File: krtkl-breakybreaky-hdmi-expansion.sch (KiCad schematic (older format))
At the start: 6 parts

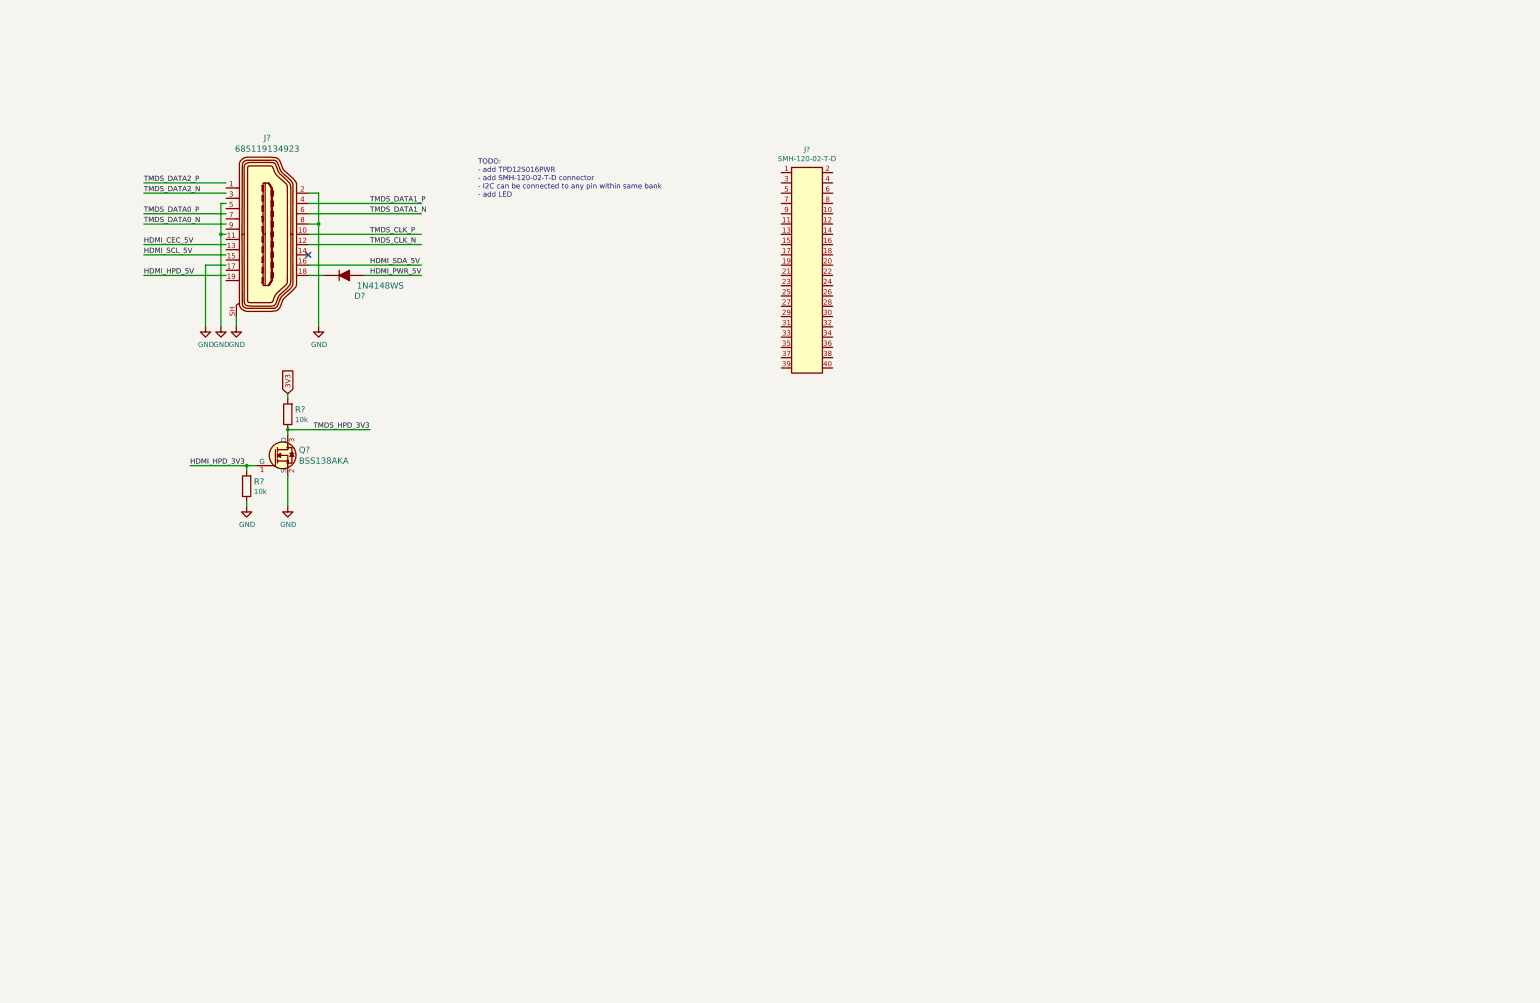
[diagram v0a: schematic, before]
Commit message: Finished schematics, added components to PCB
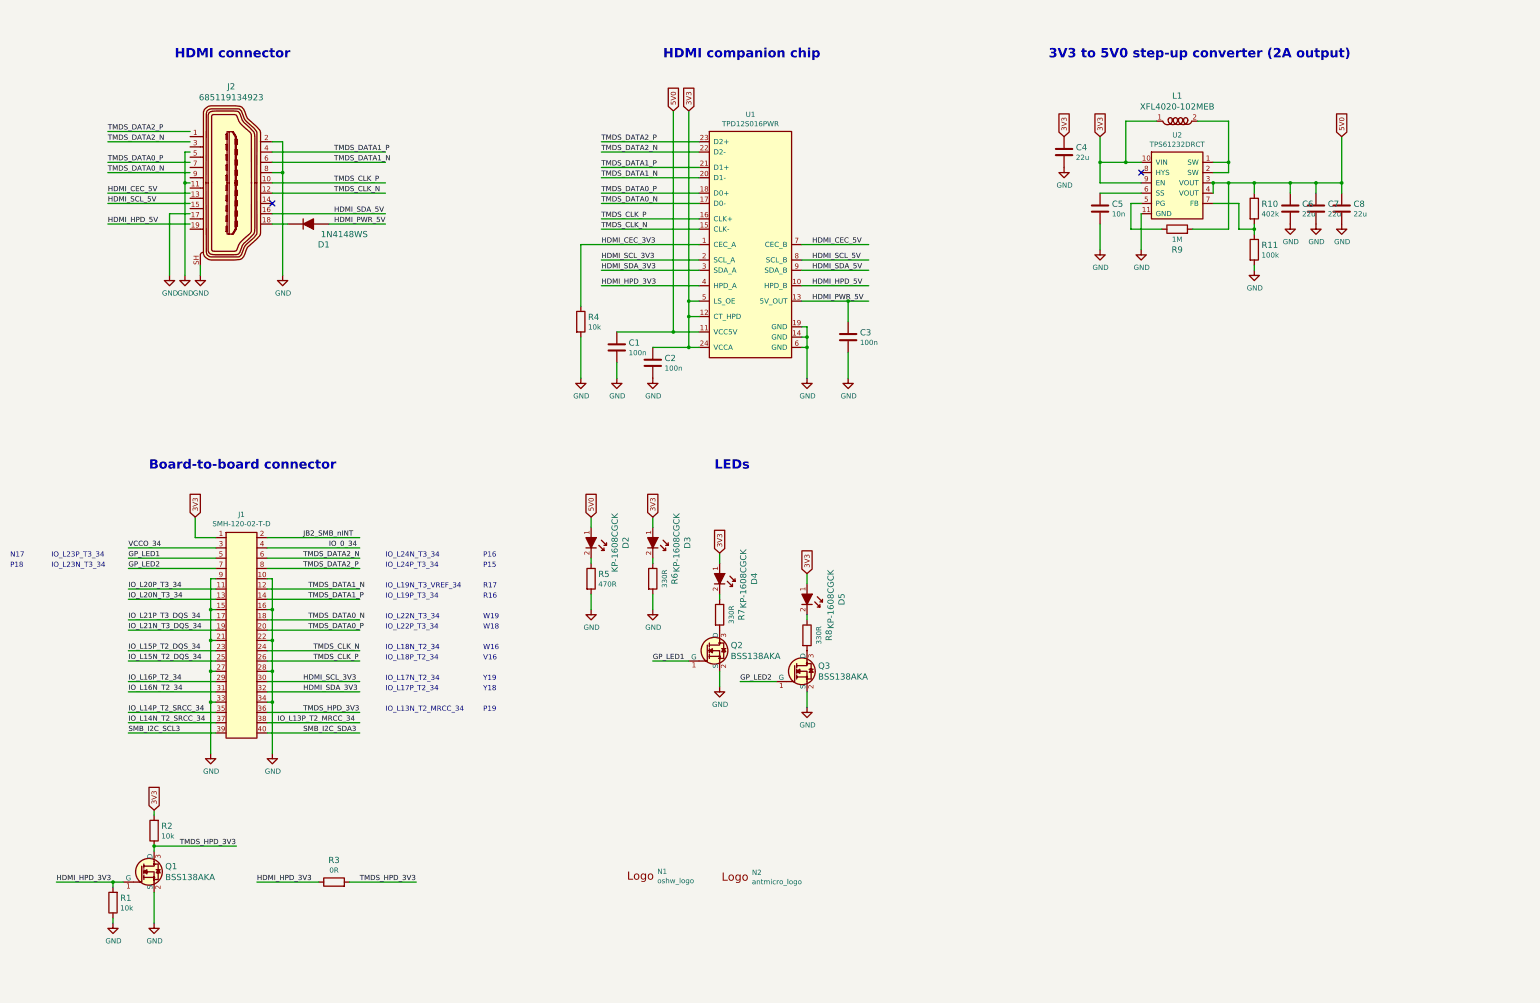
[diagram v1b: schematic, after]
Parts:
- added C1, C2, C3: C_100n_0402_6V3, antmicro-footprints:0402-cap, symbol antmicroCapacitors0402:C_100n_0402_6V3
- added C4: C_22u_0805, antmicro-footprints:0805-cap, symbol antmicroCapacitorsmisc:C_22u_0805
- added C5: C_10n_0402, antmicro-footprints:0402-cap, symbol antmicroCapacitors0402:C_10n_0402
- added C6, C7, C8: C_22u_0805_10V, antmicro-footprints:0805-cap, symbol antmicroCapacitorsmisc:C_22u_0805_10V
- added D2, D3, D4, D5: KP-1608CGCK, antmicro-footprints:LED_0603, symbol antmicroLEDIndicationDiscrete:KP-1608CGCK
- added L1: XFL4020-102MEB, antmicro-footprints:XFL4020-102MEB, symbol antmicroFixedInductors:XFL4020-102MEB
- added N1: oshw_logo, antmicro-footprints:oshw-logo, symbol antmicroMechanicalParts:oshw_logo
- added N2: antmicro_logo, antmicro-footprints:antmicro-logo_scaled_20mm, symbol antmicroMechanicalParts:antmicro_logo
- added Q2, Q3: BSS138AKA, antmicro-footprints:SOT-23-3, symbol antmicroTransistorsFETsMOSFETsSingle:BSS138AKA
- added R10: R_402k_0402, antmicro-footprints:0402-res, symbol antmicroResistors0402:R_402k_0402
- added R11: R_100k_0402, antmicro-footprints:0402-res, symbol antmicroResistors0402:R_100k_0402
- added R3: R_0R_0402, antmicro-footprints:0402-res, symbol antmicroResistors0402:R_0R_0402
- added R4: R_10k_0402, antmicro-footprints:0402-res, symbol antmicroResistors0402:R_10k_0402
- added R5: R_470R_0402, antmicro-footprints:0402-res, symbol antmicroResistors0402:R_470R_0402
- added R6, R7, R8: R_330R_0402, antmicro-footprints:0402-res, symbol antmicroResistors0402:R_330R_0402
- added R9: R_1M_0603, antmicro-footprints:0603-res, symbol antmicroResistors0603:R_1M_0603
- added U1: TPD12S016PWR, antmicro-footprints:TPD12S016PWR, symbol antmicroInterfaceControllers:TPD12S016PWR
- added U2: TPS61232DRCT, antmicro-footprints:VSON-10-1EP_3x3mm, symbol antmicroDCDCConverters:TPS61232DRCT
- gave numbers to parts that had none: 6
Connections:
- net labels added: 5V0, GP_LED1, GP_LED2, HDMI_CEC_3V3, HDMI_SCL_3V3, HDMI_SDA_3V3, IO_0_34, IO_L13P_T2_MRCC_34, IO_L14N_T2_SRCC_34, IO_L14P_T2_SRCC_34, IO_L15N_T2_DQS_34, IO_L15P_T2_DQS_34, IO_L16N_T2_34, IO_L16P_T2_34, IO_L20N_T3_34, IO_L20P_T3_34, IO_L21N_T3_DQS_34, IO_L21P_T3_DQS_34, JB2_SMB_nINT, SMB_I2C_SCL3, SMB_I2C_SDA3, VCCO_34
- wire segments 33 -> 176
- no-connect marks 1 -> 2
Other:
- note added: "3V3 to 5V0 step-up converter (2A output)"
- note added: "Board-to-board connector"
- note added: "HDMI companion chip"
- note added: "HDMI connector"
- note added: "IO_L13N_T2_MRCC_34"
- note added: "IO_L17N_T2_34"
- note added: "IO_L17P_T2_34"
- note added: "IO_L18N_T2_34"
- note added: "IO_L18P_T2_34"
- note added: "IO_L19N_T3_VREF_34"
- note added: "IO_L19P_T3_34"
- note added: "IO_L22N_T3_34"
- note added: "IO_L22P_T3_34"
- note added: "IO_L23N_T3_34"
- note added: "IO_L23P_T3_34"
- note added: "IO_L24N_T3_34"
- note added: "IO_L24P_T3_34"
- note added: "LEDs"
- note added: "N17"
- note added: "P15"
- note added: "P16"
- note added: "P18"
- note added: "P19"
- note added: "R16"
- note added: "R17"
- note added: "V16"
- note added: "W16"
- note added: "W18"
- note added: "W19"
- note added: "Y18"
- note added: "Y19"
- note removed: "TODO:\n- add TPD12S016PWR\n- add SMH-120-02-T-D connector\n- I2C can be connected to any pin within same bank\n- add LED"
- moved on the sheet: D1, J1, J2, Q1, R1, R2

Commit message: Added TODOs and some remarks
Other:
- note added: "3V3 to 5V0 step-up converter"
- note added: "General purpose LEDs driven from FPGA\n"
- note added: "Optional bypass of HPD which will not ivert logic state at this signal\n"
- note added: "Power indicators"
- note added: "Provides 5V0 system voltage for HDMI interfacing"
- note added: "TODO: Add 0R here so we can do the bringup of the DC/DC without burning the rest of the board"
- note added: "TODO: Check orientation and pinout before routing"
- note added: "TODO: Connect shields together and connect the shield ground to system GND with a BLM choke"
- note added: "TODO: Update J2 schematic symbol"
- note added: "TODO: add schematic sections, add logotypes and branding\n"
- note added: "TODO: consider adding a jumper (0R) between the 3V3 and VCCO34"
- note added: "TODO: move values"
- note added: "This connector matches the JB2 pinhead on breakyBreaky"
- note added: "max 2A"
- note removed: "3V3 to 5V0 step-up converter (2A output)"
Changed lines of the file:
@@
 LEDs
 Text Notes 10800 1500 0    91   ~ 18
-3V3 to 5V0 step-up converter (2A output)
+3V3 to 5V0 step-up converter
 Text Notes 2300 1500 0    91   ~ 18
 HDMI connector
@@
 	1    0    0    -1
 $EndComp
+Text Notes 950  1840 0    50   ~ 0
+TODO: Update J2 schematic symbol
+Text Notes 1190 4040 0    50   ~ 0
+TODO: Connect shields together and connect the shield ground to system GND with a BLM choke
+Text Notes 680  5650 0    50   ~ 0
+TODO: Check orientation and pinout before routing
+Text Notes 2610 9690 0    50   ~ 0
+Optional bypass of HPD which will not ivert logic state at this signal\n
+Text Notes 11750 9220 0    50   ~ 0
+TODO: add schematic sections, add logotypes and branding\n
+Text Notes 7430 8170 0    50   ~ 0
+General purpose LEDs driven from FPGA\n
+Text Notes 6200 7230 1    50   ~ 0
+Power indicators
+Text Notes 10790 1750 0    50   ~ 0
+Provides 5V0 system voltage for HDMI interfacing
+Text Notes 13730 2320 0    50   ~ 0
+max 2A
+Text Notes 10980 3800 0    50   ~ 0
+TODO: Add 0R here so we can do the bringup of the DC/DC without burning the rest of the board
+Text Notes 13280 3500 0    50   ~ 0
+TODO: move values
+Text Notes 690  5760 0    50   ~ 0
+TODO: consider adding a jumper (0R) between the 3V3 and VCCO34
+Text Notes 1690 8540 0    50   ~ 0
+This connector matches the JB2 pinhead on breakyBreaky
 $EndSCHEMATC

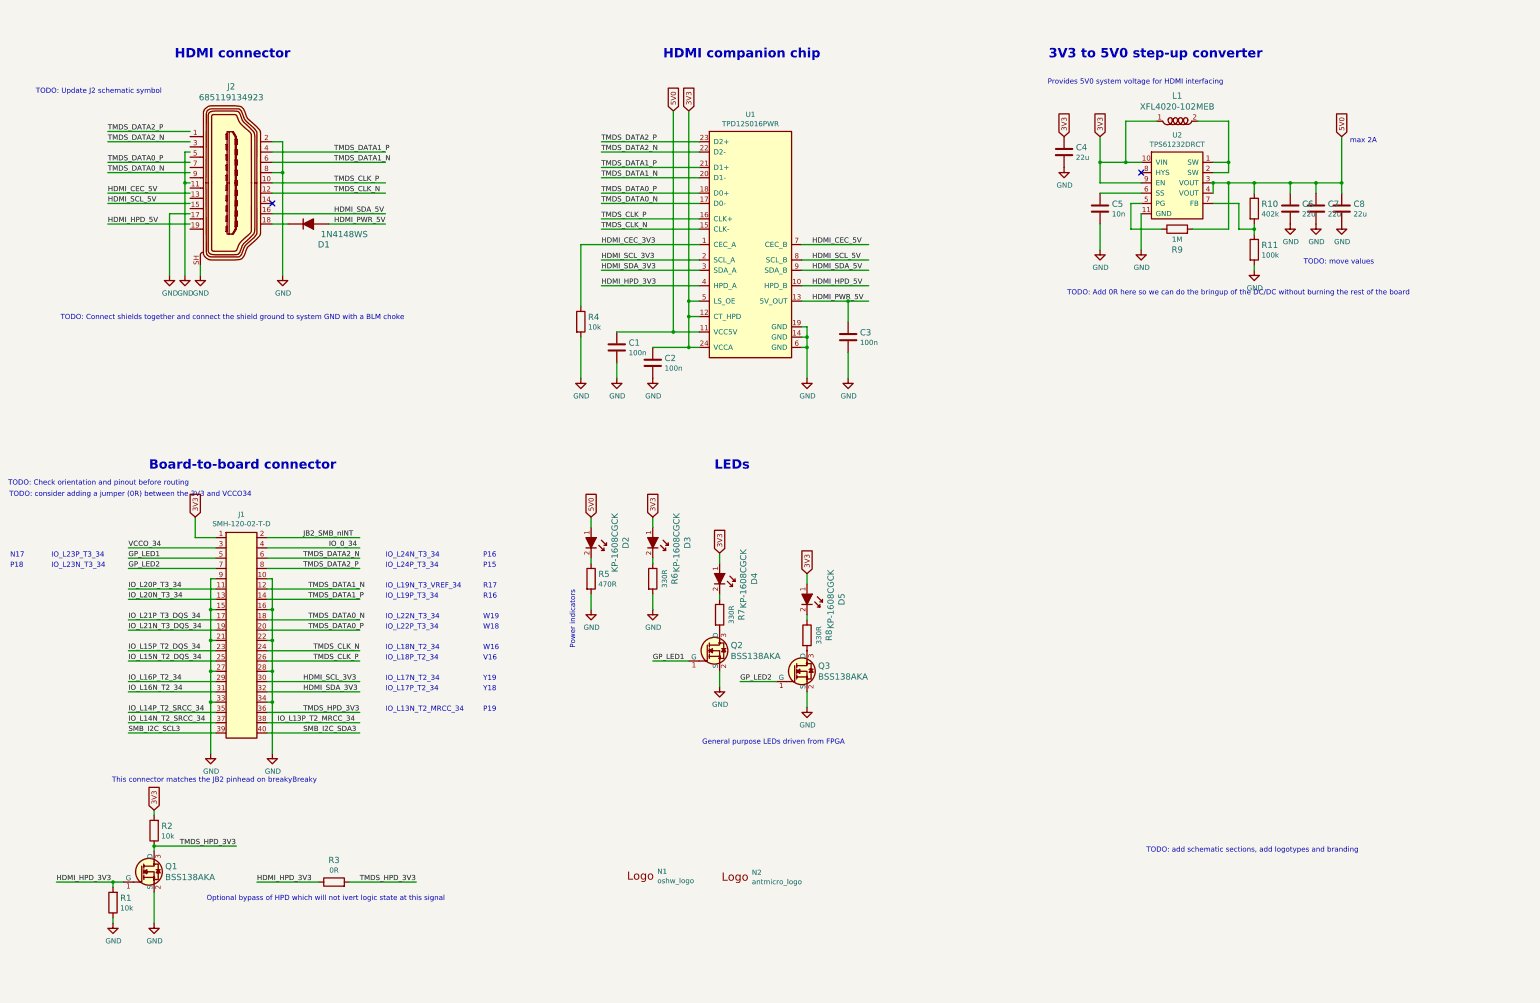
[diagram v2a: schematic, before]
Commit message: Resolved TODOs, cleaned up the schematic layout
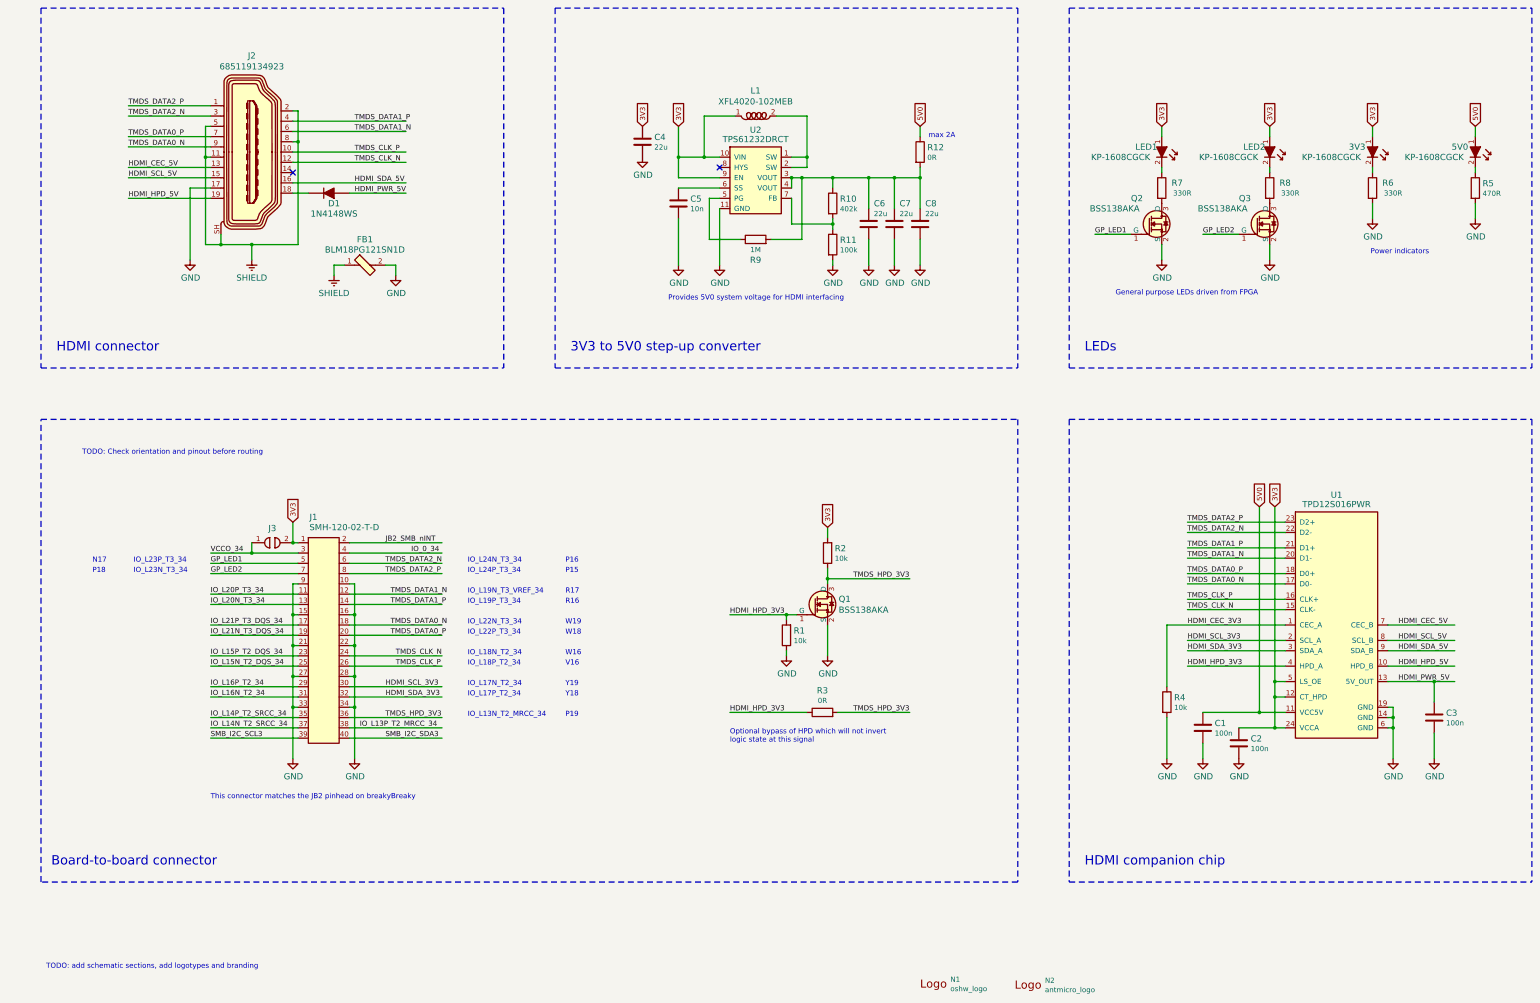
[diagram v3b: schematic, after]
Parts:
- added FB1: BLM18PG121SN1D, antmicro-footprints:0603, symbol antmicroFerriteBeadsandChips:BLM18PG121SN1D
- added J3: solder_jumper, antmicro-footprints:SolderJumper-0.6x1.4mm, symbol antmicroShuntsJumpers:solder_jumper
- added R12: R_0R_0603, antmicro-footprints:0603-res, symbol antmicroResistors0603:R_0R_0603
- added SHIELD (x2): Earth, symbol power:Earth
- renumbered D3 to 3V3, D2 to 5V0, D4 to LED1, D5 to LED2
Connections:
- wire segments 176 -> 190
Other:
- note added: "Optional bypass of HPD which will not invert \nlogic state at this signal\n"
- note removed: "Optional bypass of HPD which will not ivert logic state at this signal\n"
- note removed: "TODO: Add 0R here so we can do the bringup of the DC/DC without burning the rest of the board"
- note removed: "TODO: Connect shields together and connect the shield ground to system GND with a BLM choke"
- note removed: "TODO: Update J2 schematic symbol"
- note removed: "TODO: consider adding a jumper (0R) between the 3V3 and VCCO34"
- note removed: "TODO: move values"
- moved on the sheet: 3V3, 5V0, C1, C2, C3, C4, C5, C6, C7, C8, D1, J1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
